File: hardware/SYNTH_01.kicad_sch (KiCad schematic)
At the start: 58 parts, among them J1 RPI4_GPIO_40, J2 Conn_01x04_Pin, SW1 SW_Push_45deg, SW10 SW_Push_45deg, SW11 SW_Push_45deg, SW12 SW_Push_45deg, SW13 SW_Push_45deg, SW14 SW_Push_45deg, SW15 SW_Push_45deg, SW16 SW_Push_45deg, SW17 SW_Push_45deg, SW18 SW_Push_45deg, SW19 SW_Push_45deg, SW2 SW_Push_45deg, SW20 SW_Push_45deg, SW21 SW_Push_45deg, SW3 SW_Push_45deg, SW4 SW_Push_45deg, SW5 SW_Push_45deg, SW6 SW_Push_45deg, SW7 SW_Push_45deg, SW8 SW_Push_45deg, SW9 SW_Push_45deg, U1 MCP23017-E/SP, U2 MCP23017-E/SP

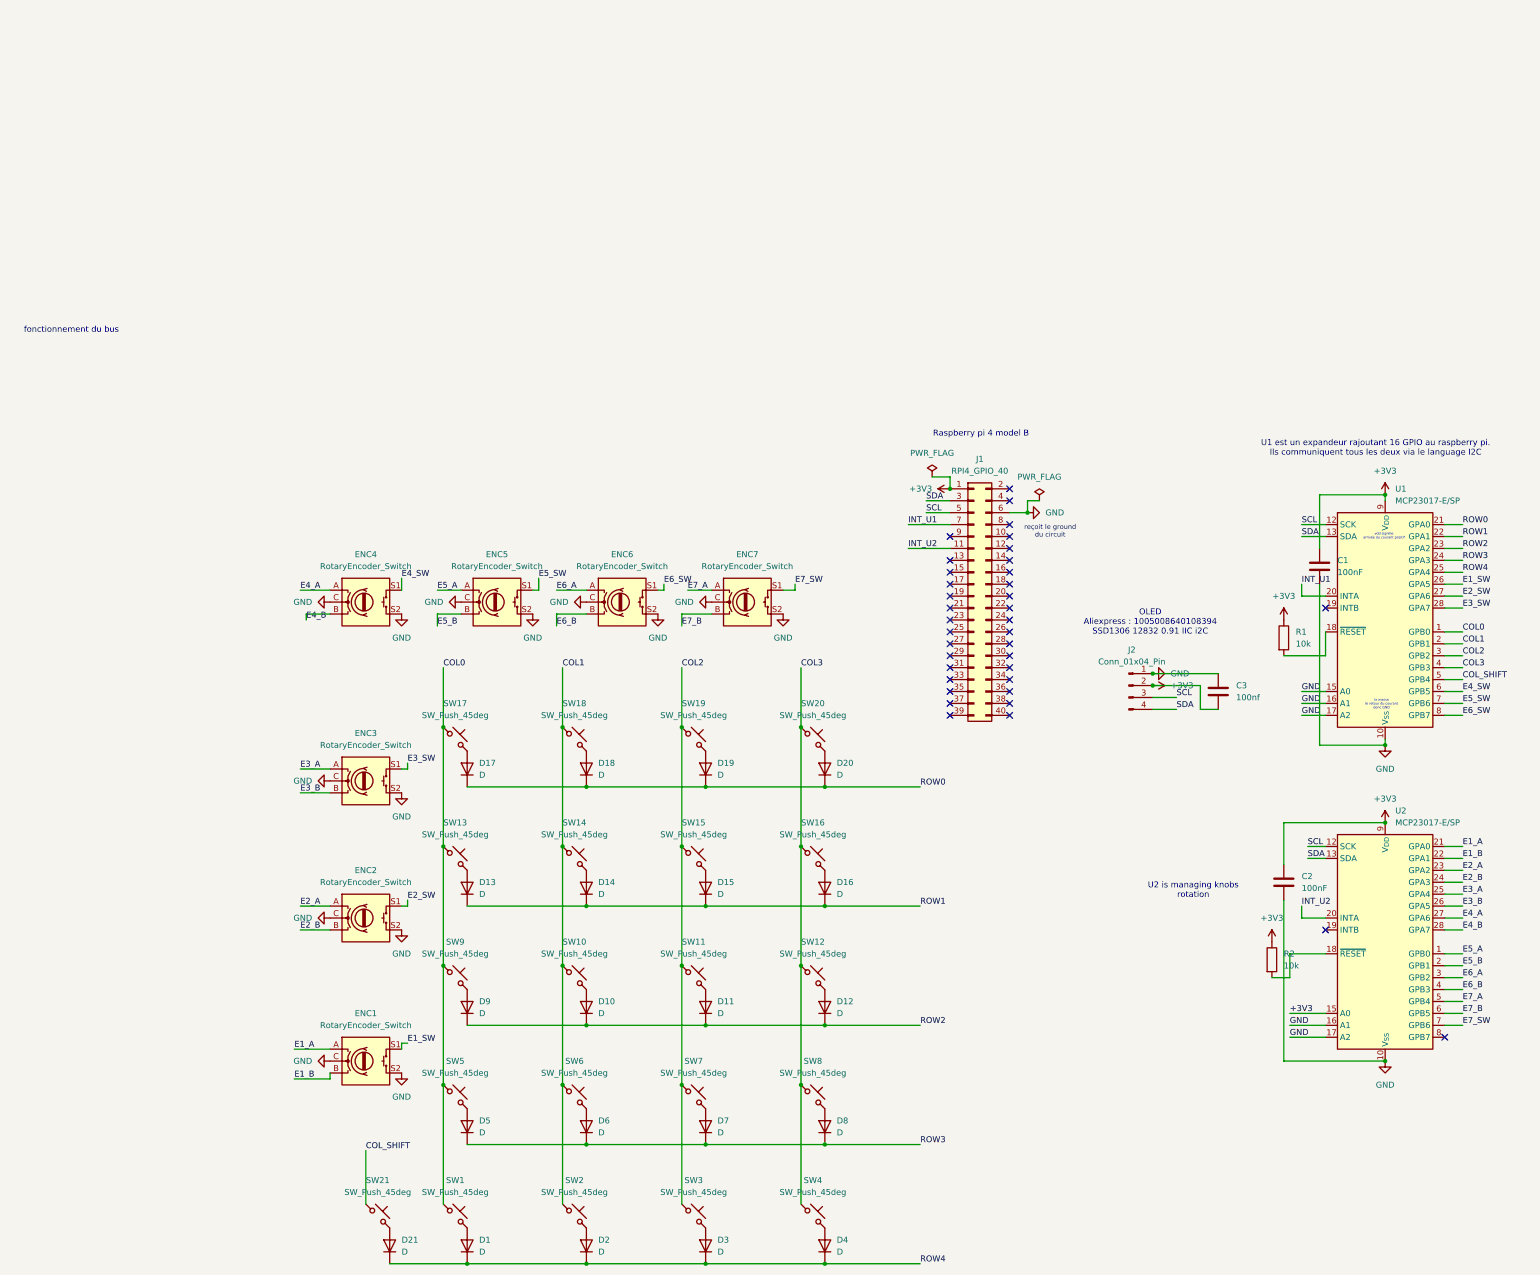
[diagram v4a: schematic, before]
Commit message: Starting PCB refactor by adding the Pico 2 H (RP2350A) into the schematic
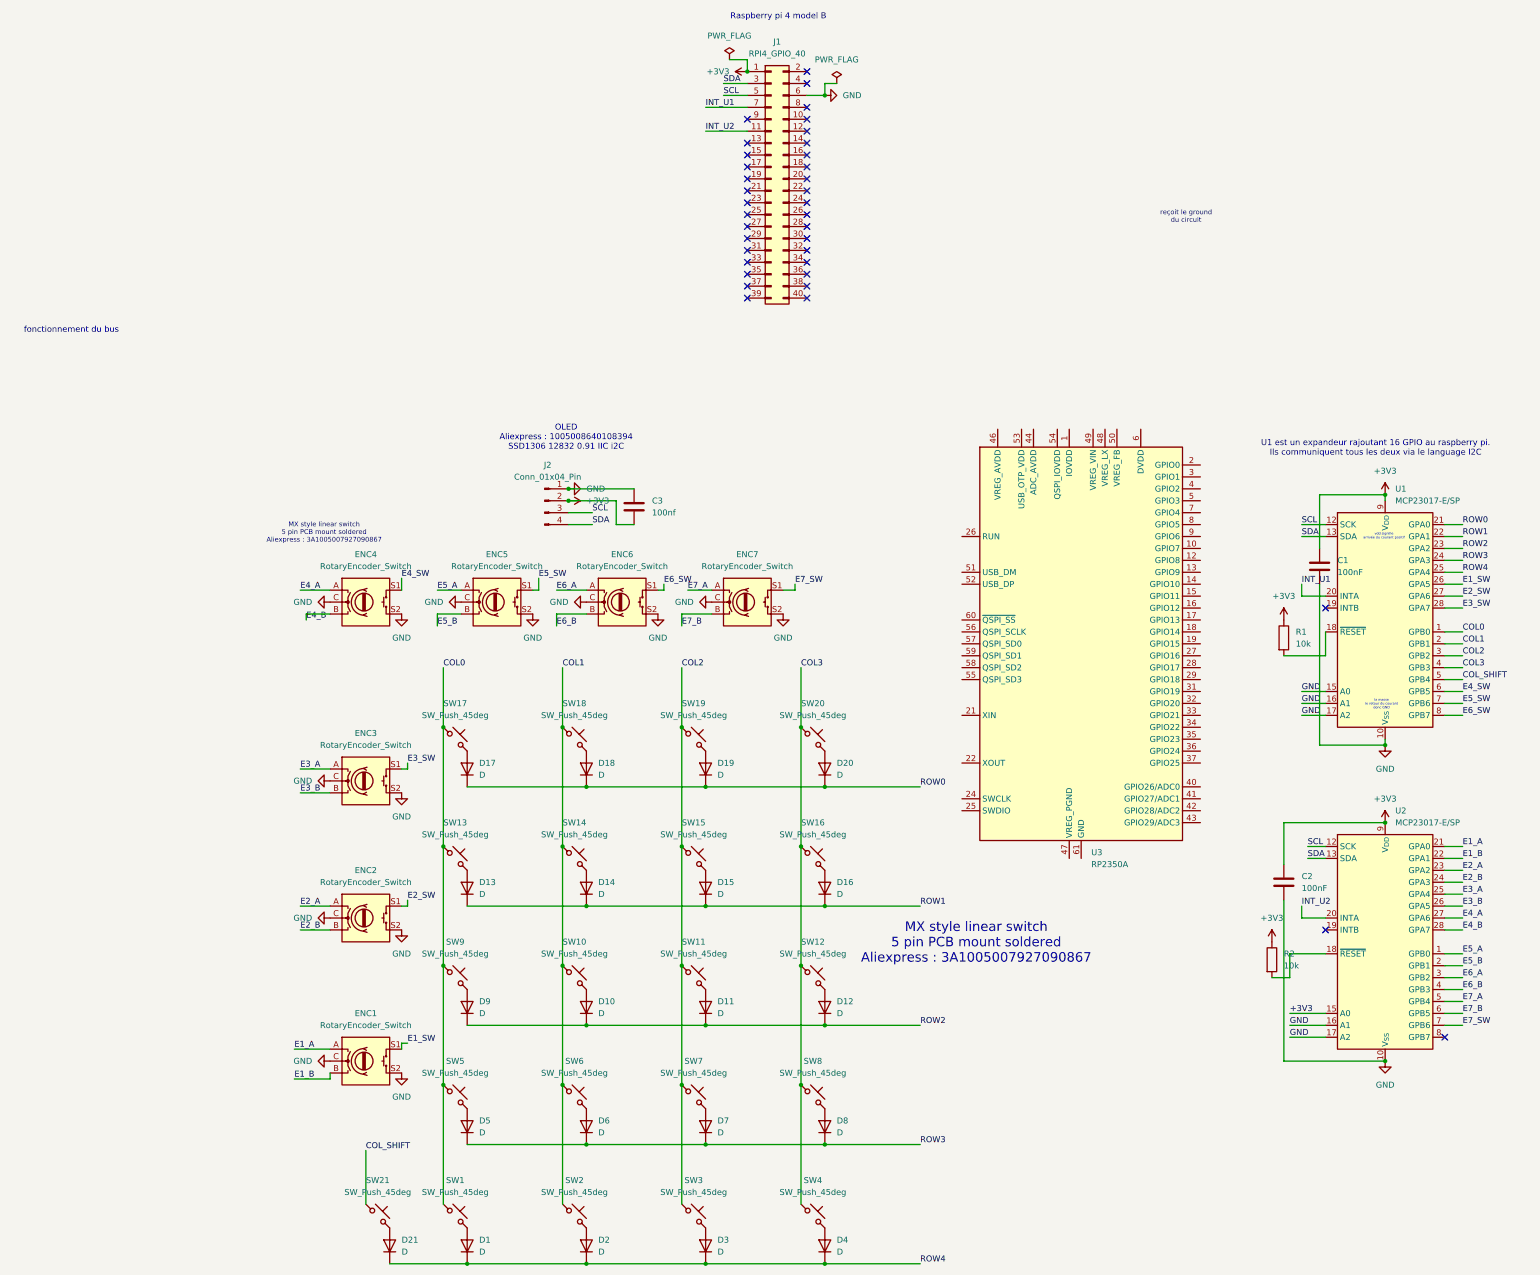
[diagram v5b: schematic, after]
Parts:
- added U3: RP2350A, Package_DFN_QFN:QFN-60-1EP_7x7mm_P0.4mm_EP3.4x3.4mm, symbol MCU_RaspberryPi:RP2350A
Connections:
- new net: U3.1 (IOVDD), U3.11 (IOVDD), U3.20 (IOVDD), U3.30 (IOVDD), U3.38 (IOVDD), U3.45 (IOVDD)
- new net: U3.23 (DVDD), U3.39 (DVDD), U3.6 (DVDD)
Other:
- note added: "MX style linear switch 5 pin PCB mount soldered Aliexpress : 3A1005007927090867"
- note removed: "U2 is managing knobs rotation"
- company: (none) -> Kowskii
- moved on the sheet: C3, J1, J2

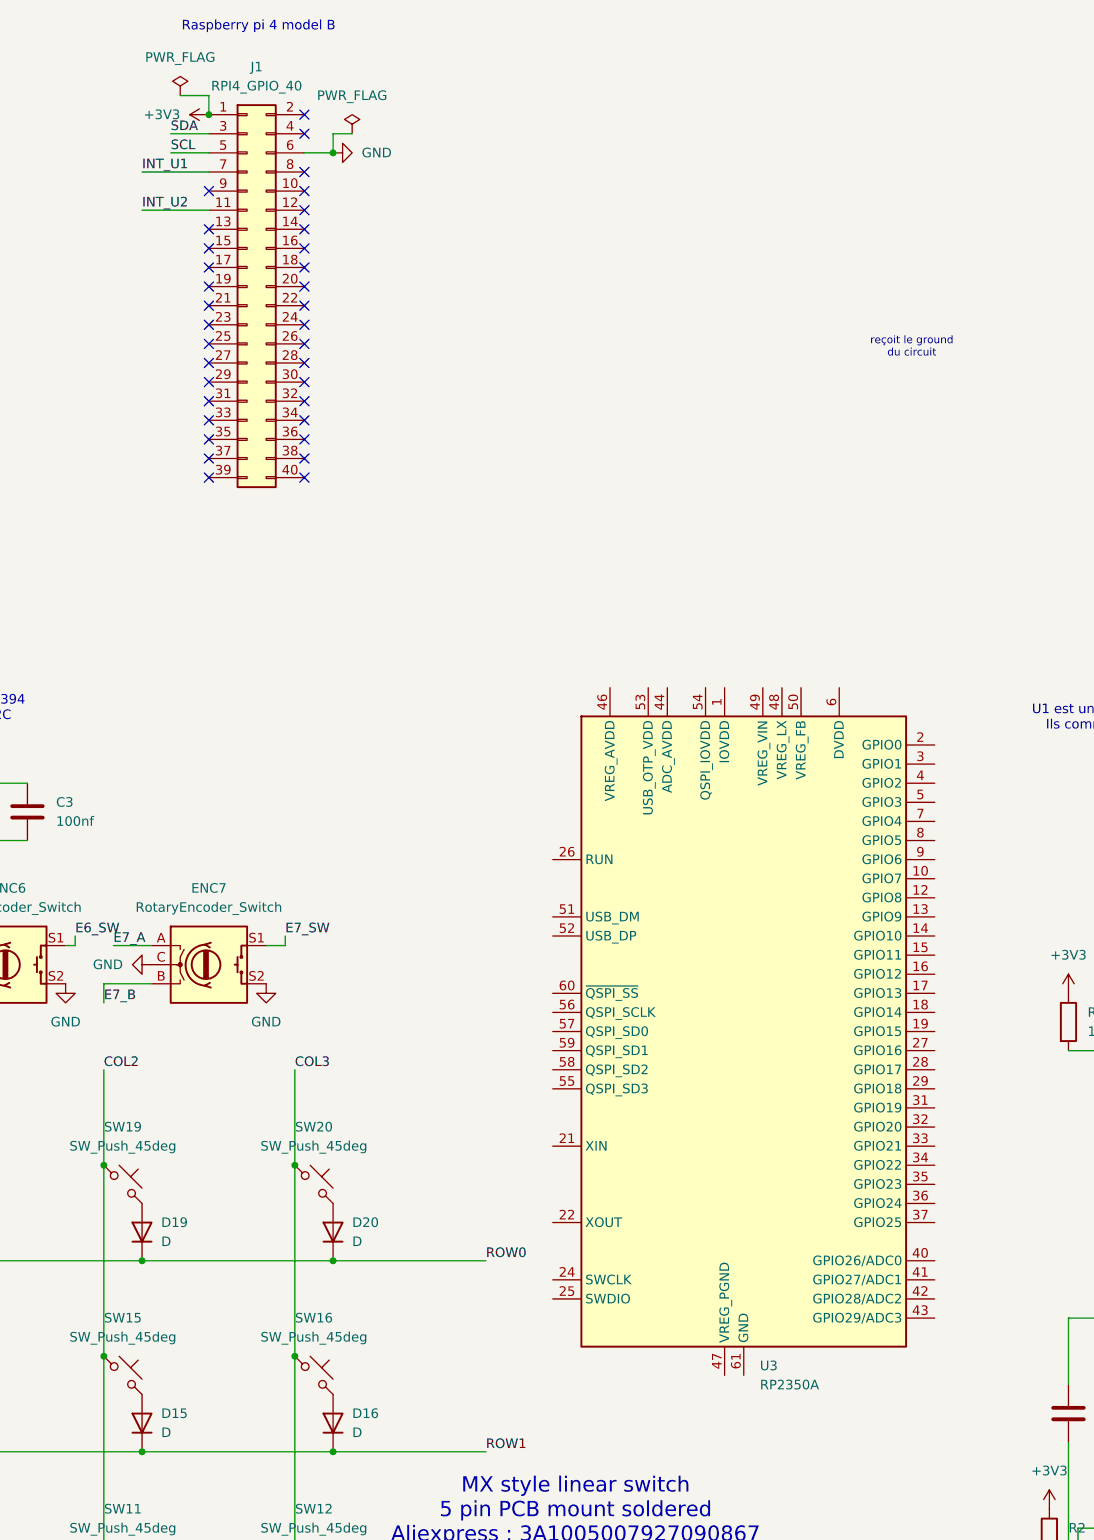
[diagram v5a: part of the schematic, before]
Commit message: [PCB] connecting power flags to pico 2, along with SDA, SCL, INT_U1, INT_U2
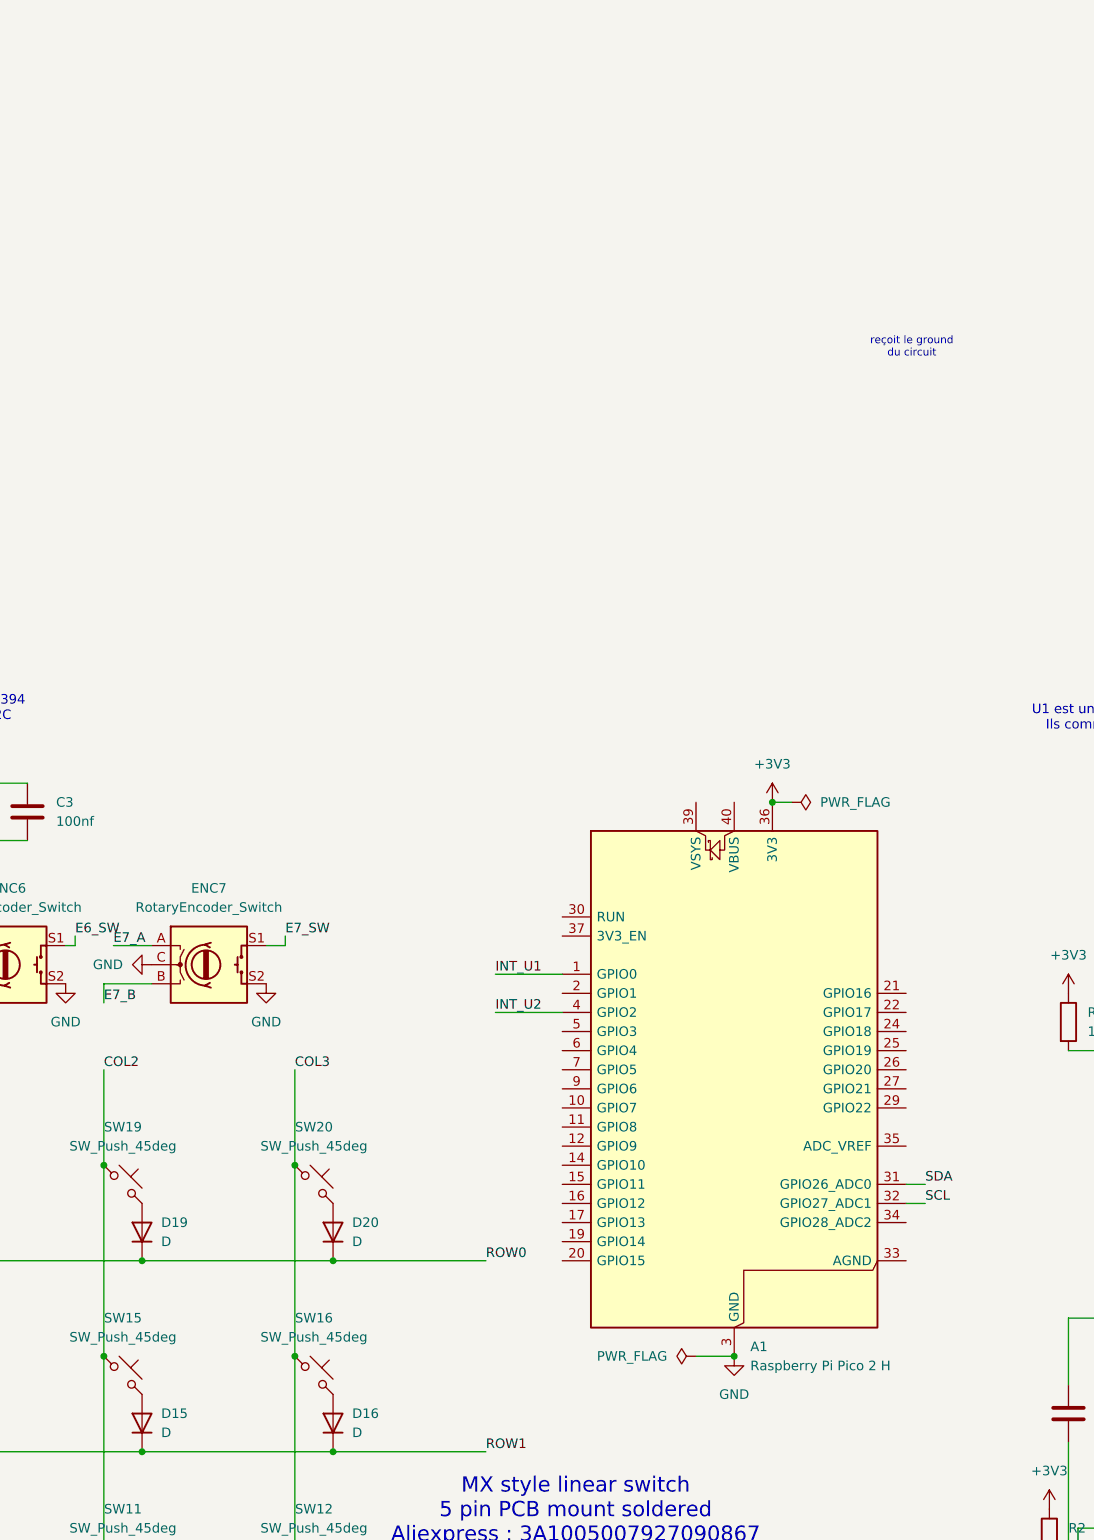
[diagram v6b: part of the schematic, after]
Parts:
- removed J1: RPI4_GPIO_40, symbol Connector_Generic:Conn_02x20_Odd_Even
- removed U3: RP2350A, Package_DFN_QFN:QFN-60-1EP_7x7mm_P0.4mm_EP3.4x3.4mm, symbol MCU_RaspberryPi:RP2350A
- added A1: Raspberry Pi Pico 2 H, Module:RaspberryPi_Pico_Common_Unspecified, symbol MCU_Module:RaspberryPi_Pico
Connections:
- net +3V3: now also A1.36 (3V3)
- net GND: now also A1.13 (GND), A1.18 (GND), A1.23 (GND), A1.28 (GND), A1.3 (GND), A1.38 (GND), A1.8 (GND)
- net INT_U1: now also A1.1 (GPIO0)
- net INT_U2: now also A1.4 (GPIO2)
- net SCL: now also A1.32 (GPIO27_ADC1)
- net SDA: now also A1.31 (GPIO26_ADC0)
- no-connect marks 37 -> 3
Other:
- note removed: "Raspberry pi 4 model B"
